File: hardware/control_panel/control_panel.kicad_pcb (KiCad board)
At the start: 2 copper layers, 70 x 37 mm, 13 parts

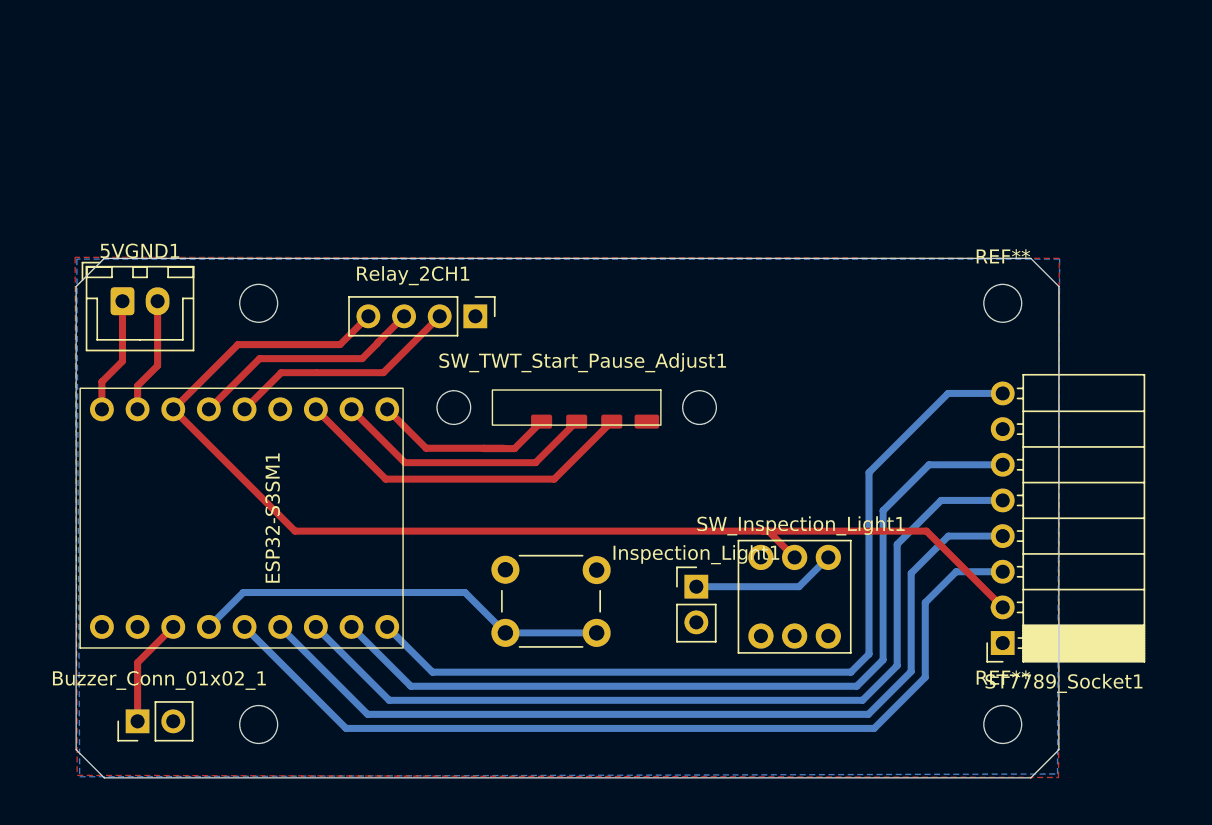
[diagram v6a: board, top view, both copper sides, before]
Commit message: KiCad - ESP32-S3 Super Mini B.Cu - Fix for flipped connections
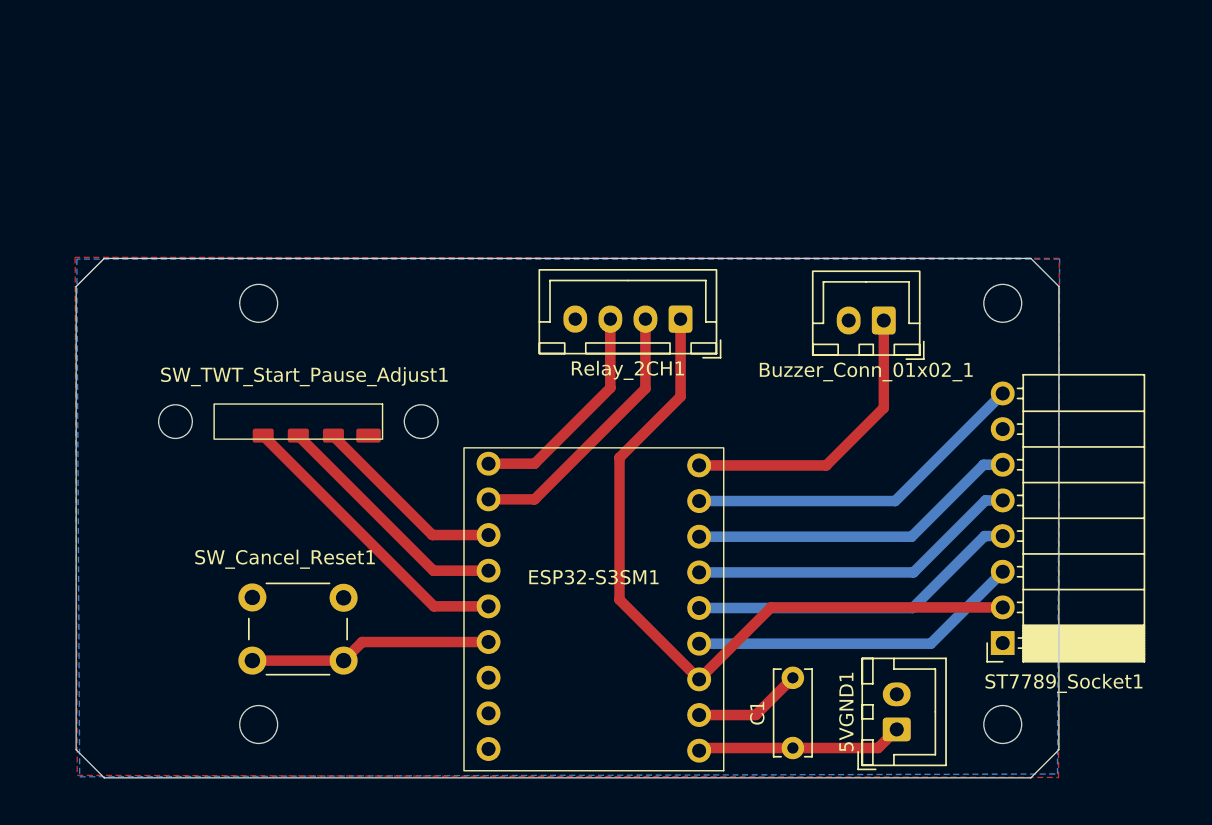
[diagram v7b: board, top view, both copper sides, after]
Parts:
- removed Inspection_Light1: Conn_01x02_Socket, Connector_PinHeader_2.54mm:PinHeader_1x02_P2.54mm_Vertical
- removed SW_Inspection_Light1: SW_Push_DPDT, TMB_Library:SW_Push_DPDT_8x8mm
- added C1: 100nF, Capacitor_THT:C_Disc_D6.0mm_W2.5mm_P5.00mm, F.Cu at (101.0, 84.9)
- Buzzer_Conn_01x02_1: footprint Connector_PinHeader_2.54mm:PinHeader_1x02_P2.54mm_Vertical -> Connector_JST:JST_XH_B2B-XH-A_1x02_P2.50mm_Vertical
- ESP32-S3SM1: footprint TMB_Library:ESP32-S3_Super_Mini_THTONLY -> TMB_Library:ESP32-S3_Super_Mini_THTONLY_(B.Cu)
- Relay_2CH1: footprint Connector_PinHeader_2.54mm:PinHeader_1x04_P2.54mm_Vertical -> Connector_JST:JST_XH_B4B-XH-A_1x04_P2.50mm_Vertical
- moved 5VGND1 63.0 mm to (108.5, 83.5), turned to 90 degrees
- moved Buzzer_Conn_01x02_1 60.3 mm to (107.5, 54.4), turned to 180 degrees
- moved ESP32-S3SM1 22.7 mm to (86.9, 72.2), turned to 180 degrees
- moved SW_TWT_Start_Pause_Adjust1 19.9 mm to (65.8, 61.6)
- moved SW_Cancel_Reset1 18.1 mm to (62.5, 74.2)
- moved Relay_2CH1 14.6 mm to (93.0, 54.3), turned to 180 degrees
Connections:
- ESP32-S3SM1 pad 1: /BUZZER -> unconnected-(ESP32-S3SM1-GP1-Pad1)
- ESP32-S3SM1 pad 10: /WH_DIR1 -> /LCD_DC
- ESP32-S3SM1 pad 11: unconnected-(ESP32-S3SM1-GP11-Pad11) -> /LCD_RST
- ESP32-S3SM1 pad 12: /IN1_FAN -> /LCD_SCL
- ESP32-S3SM1 pad 13: /IN2_LEDS -> /LCD_SDA
- ESP32-S3SM1 pad 3: /LCD_SCL -> /WH_DIR2
- ESP32-S3SM1 pad 4: /LCD_SDA -> /WH_SW
- ESP32-S3SM1 pad 5: /LCD_RST -> /WH_DIR1
- ESP32-S3SM1 pad 6: /LCD_DC -> /IN1_FAN
- ESP32-S3SM1 pad 7: /LCD_BL -> /IN2_LEDS
- ESP32-S3SM1 pad 8: /WH_DIR2 -> /BUZZER
- ESP32-S3SM1 pad 9: /WH_SW -> /LCD_BL
- Relay_2CH1 pad 1: GND -> /3V3+
- Relay_2CH1 pad 4: /3V3+ -> GND
- ST7789_Socket1 pad 3: /LCD_SCL -> /LCD_SDA
- ST7789_Socket1 pad 4: /LCD_SDA -> /LCD_SCL
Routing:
- net /LCD_SCL: track 64.7 -> 23.7 mm
- net /LCD_SDA: track 63.4 -> 23.7 mm
- net /LCD_RST: track 62.0 -> 23.7 mm
- net /LCD_DC: track 60.9 -> 23.7 mm
- net /LCD_BL: track 61.0 -> 24.8 mm
- net /3V3+: track 85.2 -> 53.6 mm
- net /BUZZER: track 7.78 -> 21.1 mm
- net /CNCL_RSET: track 29.8 -> 17.4 mm
- net /WH_DIR1: track 24.8 -> 14.0 mm
- net /INSP_LITE_3.3V+: track 10.3 -> 0.00 mm
- net /WH_DIR2: track 14.4 -> 21.1 mm
- net /+5V: track 8.31 -> 14.7 mm
- net /IN1_FAN: track 16.6 -> 19.4 mm
- net /WH_SW: track 18.8 -> 17.5 mm
- net /IN2_LEDS: track 16.7 -> 15.8 mm
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
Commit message: Fix: LCD SCL SDA mixup
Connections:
- ESP32-S3SM1 pad 12: /LCD_SCL -> /LCD_SDA
- ESP32-S3SM1 pad 13: /LCD_SDA -> /LCD_SCL
- ST7789_Socket1 pad 3: /LCD_SDA -> /LCD_SCL
- ST7789_Socket1 pad 4: /LCD_SCL -> /LCD_SDA
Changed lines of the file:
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@@
 			(layers "*.Cu" "*.Mask")
 			(remove_unused_layers no)
-			(net 10 "/LCD_SDA")
+			(net 7 "/LCD_SCL")
 			(pinfunction "Pin_3")
 			(pintype "passive")
@@
 			(layers "*.Cu" "*.Mask")
 			(remove_unused_layers no)
-			(net 7 "/LCD_SCL")
+			(net 10 "/LCD_SDA")
 			(pinfunction "Pin_4")
 			(pintype "passive")
@@
 			(layers "*.Cu" "*.Mask")
 			(remove_unused_layers no)
-			(net 7 "/LCD_SCL")
+			(net 10 "/LCD_SDA")
 			(pinfunction "GP12")
 			(pintype "bidirectional")
@@
 			(layers "*.Cu" "*.Mask")
 			(remove_unused_layers no)
-			(net 10 "/LCD_SDA")
+			(net 7 "/LCD_SCL")
 			(pinfunction "GP13")
 			(pintype "bidirectional")
@@
 	)
 	(segment
+		(start 110.875 77.445)
+		(end 116 72.32)
+		(width 0.75)
+		(layer "B.Cu")
+		(net 7)
+	)
+	(segment
+		(start 94.375 77.445)
+		(end 110.875 77.445)
+		(width 0.75)
+		(layer "B.Cu")
+		(net 7)
+	)
+	(segment
+		(start 79.375 67.165)
+		(end 82.655 67.165)
+		(width 0.75)
+		(layer "F.Cu")
+		(net 8)
+	)
+	(segment
+		(start 82.655 67.165)
+		(end 90.55 59.27)
+		(width 0.75)
+		(layer "F.Cu")
+		(net 8)
+	)
+	(segment
+		(start 90.55 59.27)
+		(end 90.55 54.325)
+		(width 0.75)
+		(layer "F.Cu")
+		(net 8)
+	)
+	(segment
 		(start 114.702596 69.78)
 		(end 116 69.78)
 		(width 0.75)
 		(layer "B.Cu")
-		(net 7)
+		(net 10)
 	)
 	(segment
@@
 		(width 0.75)
 		(layer "B.Cu")
-		(net 7)
+		(net 10)
 	)
 	(segment
@@
 		(width 0.75)
 		(layer "B.Cu")
-		(net 7)
-	)
-	(segment
-		(start 79.375 67.165)
-		(end 82.655 67.165)
-		(width 0.75)
-		(layer "F.Cu")
-		(net 8)
-	)
-	(segment
-		(start 82.655 67.165)
-		(end 90.55 59.27)
-		(width 0.75)
-		(layer "F.Cu")
-		(net 8)
-	)
-	(segment
-		(start 90.55 59.27)
-		(end 90.55 54.325)
-		(width 0.75)
-		(layer "F.Cu")
-		(net 8)
-	)
-	(segment
-		(start 110.875 77.445)
-		(end 116 72.32)
-		(width 0.75)
-		(layer "B.Cu")
-		(net 10)
-	)
-	(segment
-		(start 94.375 77.445)
-		(end 110.875 77.445)
-		(width 0.75)
-		(layer "B.Cu")
